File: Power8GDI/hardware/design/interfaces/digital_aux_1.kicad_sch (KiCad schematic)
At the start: 32 parts, among them U1600 SN74LVC14AQPWRQ1

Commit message: Integrate protected GDI and CAN wideband nodes with Huge channel allocation
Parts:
- removed C1605: 47p 100V C0G, Capacitor_SMD:C_0603_1608Metric, symbol Power8GDI_Core:C
- removed D1605: BAT54S,215, Package_TO_SOT_SMD:SOT-23, symbol Power8GDI_Core:BAT54S
- removed R1615: 10k, Resistor_SMD:R_0603_1608Metric, symbol Power8GDI_Core:R
- removed R1616: 47k, Resistor_SMD:R_0603_1608Metric, symbol Power8GDI_Core:R
- removed R1617: 10k DNP, Resistor_SMD:R_0603_1608Metric, symbol Power8GDI_Core:R
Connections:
- net DIN5_FILTERED is gone; now on net GND: U1600.13 (6A)
- net DIN5: no longer names the net of U1600.12 (6Y_INV)
- no-connect marks 0 -> 1
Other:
- note added: "HALL1..4 and FLEX_FREQ use EXTI14/15/0/7/8. Former DIN5..8 connector sites now serve MOTOR3/4. Input low/high thresholds, cable faults, power-off rail injection and flex frequency timing are not qualified. Every active channel inverts. Optional open-drain pullups remain DNP until actual sensor models are known."
- note removed: "HALL1..4 and FLEX_FREQ use EXTI14/15/0/7/8. DIN5..8 are POLLED, no EXTI reservations. Input low/high thresholds, cable faults, power-off rail injection and flex frequency timing are not qualified. Every active channel inverts. Optional open-drain pullups remain DNP until actual sensor models are known."
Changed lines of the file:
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@@
 (wire (pts (xy 474.98 261.62) (xy 474.98 269.24)) (stroke (width 0) (type default)))
 (global_label "HARNESS_FLEX_FREQ" (shape bidirectional) (at 474.98 269.24 90) (effects (font (size 1.016 1.016)) (justify right bottom)))
-(symbol (lib_id "Power8GDI_Core:R") (at 224.79 306.07 0) (unit 1) (in_bom yes) (on_board yes) (dnp no) (property "Reference" "R1615" (at 228.79 304.8 0) (effects (font (size 1.27 1.27)) (justify left))) (property "Value" "10k" (at 228.79 307.34 0) (effects (font (size 1.27 1.27)) (justify left))) (property "Footprint" "Resistor_SMD:R_0603_1608Metric" (at 224.79 306.07 0) (effects (font (size 1.27 1.27)) (hide yes))) (property "Design note" "Current limit only, no automotive pulse rating claim" (at 224.79 306.07 0) (effects (font (size 1.27 1.27)) (hide yes))) (pin "1") (pin "2") (instances (project "Power8GDI_Core" (path "/f4d21065-0a5b-5086-a08e-1af9469f04bd/7a622c8e-9078-578e-989f-4d863863197b" (reference "R1615") (unit 1)))))
-(wire (pts (xy 224.79 302.26) (xy 224.79 294.64)) (stroke (width 0) (type default)))
-(global_label "HARNESS_DIN5" (shape bidirectional) (at 224.79 294.64 270) (effects (font (size 1.016 1.016)) (justify left bottom)))
-(wire (pts (xy 224.79 309.88) (xy 224.79 317.5)) (stroke (width 0) (type default)))
-(global_label "DIN5_FILTERED" (shape bidirectional) (at 224.79 317.5 90) (effects (font (size 1.016 1.016)) (justify right bottom)))
-(symbol (lib_id "Power8GDI_Core:R") (at 284.48 306.07 0) (unit 1) (in_bom yes) (on_board yes) (dnp no) (property "Reference" "R1616" (at 288.48 304.8 0) (effects (font (size 1.27 1.27)) (justify left))) (property "Value" "47k" (at 288.48 307.34 0) (effects (font (size 1.27 1.27)) (justify left))) (property "Footprint" "Resistor_SMD:R_0603_1608Metric" (at 284.48 306.07 0) (effects (font (size 1.27 1.27)) (hide yes))) (property "Design note" "" (at 284.48 306.07 0) (effects (font (size 1.27 1.27)) (hide yes))) (pin "1") (pin "2") (instances (project "Power8GDI_Core" (path "/f4d21065-0a5b-5086-a08e-1af9469f04bd/7a622c8e-9078-578e-989f-4d863863197b" (reference "R1616") (unit 1)))))
-(wire (pts (xy 284.48 302.26) (xy 284.48 294.64)) (stroke (width 0) (type default)))
-(global_label "DIN5_FILTERED" (shape bidirectional) (at 284.48 294.64 270) (effects (font (size 1.016 1.016)) (justify left bottom)))
-(wire (pts (xy 284.48 309.88) (xy 284.48 317.5)) (stroke (width 0) (type default)))
-(global_label "GND" (shape bidirectional) (at 284.48 317.5 90) (effects (font (size 1.016 1.016)) (justify right bottom)))
-(symbol (lib_id "Power8GDI_Core:C") (at 345.44 306.07 0) (unit 1) (in_bom yes) (on_board yes) (dnp no) (property "Reference" "C1605" (at 349.44 304.8 0) (effects (font (size 1.27 1.27)) (justify left))) (property "Value" "47p 100V C0G" (at 349.44 307.34 0) (effects (font (size 1.27 1.27)) (justify left))) (property "Footprint" "Capacitor_SMD:C_0603_1608Metric" (at 345.44 306.07 0) (effects (font (size 1.27 1.27)) (hide yes))) (property "Design note" "Nominal RC0.39us; actual source/cable/Schmitt delays require timing validation" (at 345.44 306.07 0) (effects (font (size 1.27 1.27)) (hide yes))) (pin "1") (pin "2") (instances (project "Power8GDI_Core" (path "/f4d21065-0a5b-5086-a08e-1af9469f04bd/7a622c8e-9078-578e-989f-4d863863197b" (reference "C1605") (unit 1)))))
-(wire (pts (xy 345.44 302.26) (xy 345.44 294.64)) (stroke (width 0) (type default)))
-(global_label "DIN5_FILTERED" (shape bidirectional) (at 345.44 294.64 270) (effects (font (size 1.016 1.016)) (justify left bottom)))
-(wire (pts (xy 345.44 309.88) (xy 345.44 317.5)) (stroke (width 0) (type default)))
-(global_label "GND" (shape bidirectional) (at 345.44 317.5 90) (effects (font (size 1.016 1.016)) (justify right bottom)))
-(symbol (lib_id "Power8GDI_Core:BAT54S") (at 405.13 306.07 0) (unit 1) (in_bom yes) (on_board yes) (dnp no) (property "Reference" "D1605" (at 405.13 293.37 0) (effects (font (size 1.27 1.27)))) (property "Value" "BAT54S,215" (at 425.45 318.77 0) (effects (font (size 1.27 1.27)) (justify left))) (property "Footprint" "Package_TO_SOT_SMD:SOT-23" (at 405.13 306.07 0) (effects (font (size 1.27 1.27)) (hide yes))) (property "Design note" "Input5.5V tolerant; clamps can inject into5V rail. Unpowered simultaneous faults block release" (at 405.13 306.07 0) (effects (font (size 1.27 1.27)) (hide yes))) (pin "1") (pin "2") (pin "3") (instances (project "Power8GDI_Core" (path "/f4d21065-0a5b-5086-a08e-1af9469f04bd/7a622c8e-9078-578e-989f-4d863863197b" (reference "D1605") (unit 1)))))
-(wire (pts (xy 405.13 316.23) (xy 405.13 323.85)) (stroke (width 0) (type default)))
-(global_label "GND" (shape bidirectional) (at 405.13 323.85 90) (effects (font (size 1.016 1.016)) (justify right bottom)))
-(wire (pts (xy 405.13 295.91) (xy 405.13 288.29)) (stroke (width 0) (type default)))
-(global_label "+5V_CORE" (shape bidirectional) (at 405.13 288.29 270) (effects (font (size 1.016 1.016)) (justify left bottom)))
-(wire (pts (xy 394.97 306.07) (xy 387.35 306.07)) (stroke (width 0) (type default)))
-(global_label "DIN5_FILTERED" (shape bidirectional) (at 387.35 306.07 0) (effects (font (size 1.016 1.016)) (justify right bottom)))
-(symbol (lib_id "Power8GDI_Core:R") (at 474.98 306.07 0) (unit 1) (in_bom yes) (on_board yes) (dnp yes) (property "Reference" "R1617" (at 478.98 304.8 0) (effects (font (size 1.27 1.27)) (justify left))) (property "Value" "10k DNP" (at 478.98 307.34 0) (effects (font (size 1.27 1.27)) (justify left))) (property "Footprint" "Resistor_SMD:R_0603_1608Metric" (at 474.98 306.07 0) (effects (font (size 1.27 1.27)) (hide yes))) (property "Design note" "Optional open-drain sensor pullup; fit only after sensor/wiring review" (at 474.98 306.07 0) (effects (font (size 1.27 1.27)) (hide yes))) (pin "1") (pin "2") (instances (project "Power8GDI_Core" (path "/f4d21065-0a5b-5086-a08e-1af9469f04bd/7a622c8e-9078-578e-989f-4d863863197b" (reference "R1617") (unit 1)))))
-(wire (pts (xy 474.98 302.26) (xy 474.98 294.64)) (stroke (width 0) (type default)))
-(global_label "+5V_CORE" (shape bidirectional) (at 474.98 294.64 270) (effects (font (size 1.016 1.016)) (justify left bottom)))
-(wire (pts (xy 474.98 309.88) (xy 474.98 317.5)) (stroke (width 0) (type default)))
-(global_label "HARNESS_DIN5" (shape bidirectional) (at 474.98 317.5 90) (effects (font (size 1.016 1.016)) (justify right bottom)))
 (symbol (lib_id "Power8GDI_Core:SN74LVC14A_Q1") (at 90.17 95.25 0) (unit 1) (in_bom yes) (on_board yes) (dnp no) (property "Reference" "U1600" (at 90.17 67.31 0) (effects (font (size 1.27 1.27)))) (property "Value" "SN74LVC14AQPWRQ1" (at 110.49000000000001 123.19 0) (effects (font (size 1.27 1.27)) (justify left))) (property "Footprint" "Package_SO:TSSOP-14_4.4x5mm_P0.65mm" (at 90.17 95.25 0) (effects (font (size 1.27 1.27)) (hide yes))) (property "Design note" "2..3.6V supply,5.5V tolerant inputs, all channels INVERT. Unused inputsGND and outputsNC" (at 90.17 95.25 0) (effects (font (size 1.27 1.27)) (hide yes))) (pin "14") (pin "7") (pin "1") (pin "2") (pin "3") (pin "4") (pin "5") (pin "6") (pin "9") (pin "8") (pin "11") (pin "10") (pin "13") (pin "12") (instances (project "Power8GDI_Core" (path "/f4d21065-0a5b-5086-a08e-1af9469f04bd/7a622c8e-9078-578e-989f-4d863863197b" (reference "U1600") (unit 1)))))
 (wire (pts (xy 90.17 69.85) (xy 90.17 62.23)) (stroke (width 0) (type default)))
@@
 (global_label "FLEX_FREQ" (shape bidirectional) (at 113.03 106.68 180) (effects (font (size 1.016 1.016)) (justify left bottom)))
 (wire (pts (xy 74.93 114.3) (xy 67.31 114.3)) (stroke (width 0) (type default)))
-(global_label "DIN5_FILTERED" (shape bidirectional) (at 67.31 114.3 0) (effects (font (size 1.016 1.016)) (justify right bottom)))
-(wire (pts (xy 105.41 114.3) (xy 113.03 114.3)) (stroke (width 0) (type default)))
-(global_label "DIN5" (shape bidirectional) (at 113.03 114.3 180) (effects (font (size 1.016 1.016)) (justify left bottom)))
+(global_label "GND" (shape bidirectional) (at 67.31 114.3 0) (effects (font (size 1.016 1.016)) (justify right bottom)))
+(no_connect (at 105.41 114.3))
 (symbol (lib_id "Power8GDI_Core:C") (at 90.17 160.02 0) (unit 1) (in_bom yes) (on_board yes) (dnp no) (property "Reference" "C1610" (at 94.17 158.75 0) (effects (font (size 1.27 1.27)) (justify left))) (property "Value" "100n 16V X7R" (at 94.17 161.29 0) (effects (font (size 1.27 1.27)) (justify left))) (property "Footprint" "Capacitor_SMD:C_0603_1608Metric" (at 90.17 160.02 0) (effects (font (size 1.27 1.27)) (hide yes))) (property "Design note" "" (at 90.17 160.02 0) (effects (font (size 1.27 1.27)) (hide yes))) (pin "1") (pin "2") (instances (project "Power8GDI_Core" (path "/f4d21065-0a5b-5086-a08e-1af9469f04bd/7a622c8e-9078-578e-989f-4d863863197b" (reference "C1610") (unit 1)))))
 (wire (pts (xy 90.17 156.21) (xy 90.17 148.59)) (stroke (width 0) (type default)))
@@
 (wire (pts (xy 90.17 163.83) (xy 90.17 171.45)) (stroke (width 0) (type default)))
 (global_label "GND" (shape bidirectional) (at 90.17 171.45 90) (effects (font (size 1.016 1.016)) (justify right bottom)))
-(text "HALL1..4 and FLEX_FREQ use EXTI14/15/0/7/8. DIN5..8 are POLLED, no EXTI reservations.\nInput low/high thresholds, cable faults, power-off rail injection and flex frequency timing are not qualified.\nEvery active channel inverts. Optional open-drain pullups remain DNP until actual sensor models are known." (at 25.4 370 0) (effects (font (size 1.27 1.27)) (justify left top)))
+(text "HALL1..4 and FLEX_FREQ use EXTI14/15/0/7/8. Former DIN5..8 connector sites now serve MOTOR3/4.\nInput low/high thresholds, cable faults, power-off rail injection and flex frequency timing are not qualified.\nEvery active channel inverts. Optional open-drain pullups remain DNP until actual sensor models are known." (at 25.4 370 0) (effects (font (size 1.27 1.27)) (justify left top)))
 (sheet_instances (path "/" (page "1"))))

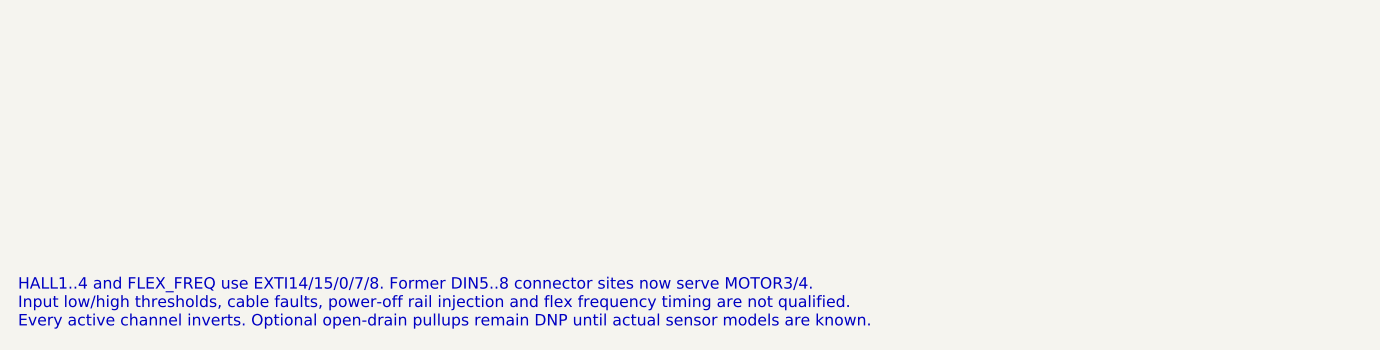
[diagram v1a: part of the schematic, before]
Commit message: Redesign sport target as six DI/PI channels with two motors and one lambda
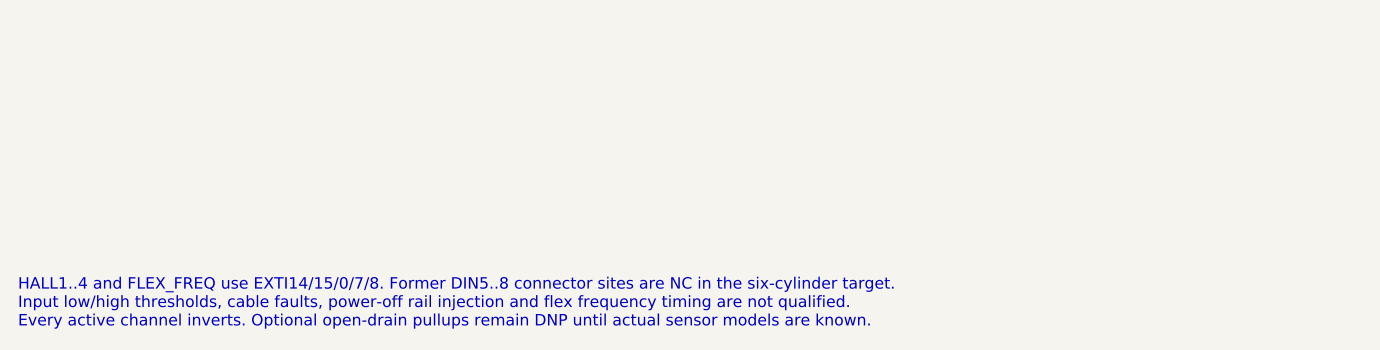
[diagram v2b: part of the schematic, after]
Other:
- note added: "HALL1..4 and FLEX_FREQ use EXTI14/15/0/7/8. Former DIN5..8 connector sites are NC in the six-cylinder target. Input low/high thresholds, cable faults, power-off rail injection and flex frequency timing are not qualified. Every active channel inverts. Optional open-drain pullups remain DNP until actual sensor models are known."
- note removed: "HALL1..4 and FLEX_FREQ use EXTI14/15/0/7/8. Former DIN5..8 connector sites now serve MOTOR3/4. Input low/high thresholds, cable faults, power-off rail injection and flex frequency timing are not qualified. Every active channel inverts. Optional open-drain pullups remain DNP until actual sensor models are known."
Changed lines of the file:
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@@
 (wire (pts (xy 90.17 163.83) (xy 90.17 171.45)) (stroke (width 0) (type default)))
 (global_label "GND" (shape bidirectional) (at 90.17 171.45 90) (effects (font (size 1.016 1.016)) (justify right bottom)))
-(text "HALL1..4 and FLEX_FREQ use EXTI14/15/0/7/8. Former DIN5..8 connector sites now serve MOTOR3/4.\nInput low/high thresholds, cable faults, power-off rail injection and flex frequency timing are not qualified.\nEvery active channel inverts. Optional open-drain pullups remain DNP until actual sensor models are known." (at 25.4 370 0) (effects (font (size 1.27 1.27)) (justify left top)))
+(text "HALL1..4 and FLEX_FREQ use EXTI14/15/0/7/8. Former DIN5..8 connector sites are NC in the six-cylinder target.\nInput low/high thresholds, cable faults, power-off rail injection and flex frequency timing are not qualified.\nEvery active channel inverts. Optional open-drain pullups remain DNP until actual sensor models are known." (at 25.4 370 0) (effects (font (size 1.27 1.27)) (justify left top)))
 (sheet_instances (path "/" (page "1"))))

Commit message: Review B58 injector power stage and bind selected GDI6 BOM
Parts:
- C1600, C1601, C1602, C1603, C1604: Hardware_Qualification (none) -> BOARD_QUALIFICATION_PENDING; MPN (none) -> C0603C470J1GACTU; Manufacturer (none) -> KEMET; Procurement_Status (none) -> SELECTED_CATALOG_ITEM; Purchase_Released (none) -> false; Selection_Gaps (none) -> []; Selection_ID (none) -> SEL-df424528ff57; Selection_Ratings (none) -> {"capacitance_pf": 47, "dielectric": "C0G", "rated_voltage_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; Selection_Source_URLs (none) -> https://www.digikey.com/en/products/detail/kemet/C0603C470J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
- C1610: Hardware_Qualification (none) -> BOARD_QUALIFICATION_PENDING; MPN (none) -> C0603C104K5RACTU; Manufacturer (none) -> KEMET; Procurement_Status (none) -> SELECTED_CATALOG_ITEM; Purchase_Released (none) -> false; Selection_Gaps (none) -> []; Selection_ID (none) -> SEL-6bf9727c4e40; Selection_Ratings (none) -> {"capacitance_pf": 100000, "dielectric": "X7R", "rated_volt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; Selection_Source_URLs (none) -> https://search.kemet.com/download/specsheet/C0603C104K5RACTU
- D1600, D1601, D1602, D1603, D1604: Hardware_Qualification (none) -> PINOUT_RATINGS_AND_DELIVERY_SUFFIX_REVIEW_PENDING; MPN (none) -> BAT54S,215; Manufacturer (none) -> Nexperia; Procurement_Status (none) -> REFERENCE_MPN_RETAINED; Purchase_Released (none) -> false; Selection_Gaps (none) -> ["Existing schematic MPN retained. Complete circuit rating/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; Selection_ID (none) -> SEL-b62e273620d3; Selection_Ratings (none) -> {}; Selection_Source_URLs (none) -> https://www.nexperia.com/product/BAT54S
- R1600, R1603, R1606, R1609, R1612: Hardware_Qualification (none) -> BOARD_QUALIFICATION_PENDING; MPN (none) -> CRCW060310K0FKEA; Manufacturer (none) -> Vishay; Procurement_Status (none) -> SELECTED_FAMILY_CODE; Purchase_Released (none) -> false; Selection_Gaps (none) -> []; Selection_ID (none) -> SEL-9c0806476875; Selection_Ratings (none) -> {"aec_q200": true, "derating": "Use manufacturer power vers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; Selection_Source_URLs (none) -> https://www.vishay.com/docs/20035/dcrcwe3.pdf
- R1601, R1604, R1607, R1610, R1613: Hardware_Qualification (none) -> BOARD_QUALIFICATION_PENDING; MPN (none) -> CRCW060347K0FKEA; Manufacturer (none) -> Vishay; Procurement_Status (none) -> SELECTED_FAMILY_CODE; Purchase_Released (none) -> false; Selection_Gaps (none) -> []; Selection_ID (none) -> SEL-8ba99d730f8b; Selection_Ratings (none) -> {"aec_q200": true, "derating": "Use manufacturer power vers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; Selection_Source_URLs (none) -> https://www.vishay.com/docs/20035/dcrcwe3.pdf
- U1600: Hardware_Qualification (none) -> PINOUT_RATINGS_AND_DELIVERY_SUFFIX_REVIEW_PENDING; MPN (none) -> SN74LVC14AQPWRQ1; Manufacturer (none) -> Texas Instruments; Procurement_Status (none) -> REFERENCE_MPN_RETAINED; Purchase_Released (none) -> false; Selection_Gaps (none) -> ["Existing schematic MPN retained. Complete circuit rating/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; Selection_ID (none) -> SEL-90b5d0e9725e; Selection_Ratings (none) -> {}; Selection_Source_URLs (none) -> https://www.ti.com/product/SN74LVC14A-Q1/part-details/SN74L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
